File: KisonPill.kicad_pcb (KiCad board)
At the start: 4 copper layers, 49 x 48 mm, 44 parts, among them J1 USB_C_Receptacle_USB2.0, J2 Conn_01x17_Male, J3 Conn_01x17_Male, J4 Conn_01x03_Male, J5 Conn_01x04_Male, J6 Conn_01x03_Male, J7 Conn_01x08_Male, Q1 2N3904S-RTK/PS, Q2 2N3904S-RTK/PS, SW1 SW_Push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

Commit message: Add Elaina
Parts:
- added G***: LOGO, KisonCommon:ElainaLogo, B.Cu at (146.8, 103.6)
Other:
- board text added: "3V3"
- board text added: "EXT_5V"
- board text added: "GND"
- board text added: "JLCJLCJLCJLC"
- board text added: "KisonHe KisonPillV0.1"

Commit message: save
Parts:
- removed G***: LOGO, KisonCommon:ElainaLogo
- added R14: 0, Resistor_SMD:R_0603_1608Metric, F.Cu at (150.2, 84.3)
- added R15: 0, Resistor_SMD:R_0603_1608Metric, F.Cu at (152.0, 84.2)
- added U7: ESP32FullConnector, Connector_Molex:Molex_CLIK-Mate_502382-1270_1x12-1MP_P1.25mm_Vertical, B.Cu at (160.1, 112.8)
- U4: value ESP32JtagConnector -> ESP32FullConnector-KisonCommon; footprint KisonCommon:jtag1.27 -> KisonCommon:jtag1.27-12
- U6: moved to B.Cu
- moved D5 5.57 mm to (143.4, 120.4), turned to 0 degrees
- moved SW1 4.63 mm to (146.8, 121.0), turned to 0 degrees
- moved C8 3.67 mm to (157.4, 85.2), turned to 270 degrees
- moved U6 3.43 mm to (143.3, 118.0), turned to 270 degrees
- moved J6 3.40 mm to (154.4, 114.3)
- moved J5 2.72 mm to (150.6, 112.1)
- moved J4 2.10 mm to (146.9, 114.2)
- moved C9 0.43 mm to (155.0, 84.5), turned to 270 degrees
- moved U4 0.16 mm to (136.9, 83.6)
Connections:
- J7 pad 6: /IO15 -> /IO32
- Q2 pad 1: /IO0 -> /DTR
- Q2 pad 3: /DTR -> /IO0
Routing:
- net /IO32: track 11.9 -> 62.0 mm, vias 0 -> 1
- net /EXT_5V: track 39.4 -> 88.3 mm
- net /EN: track 134.0 -> 94.5 mm
- net +3V3: track 189.8 -> 168.3 mm, vias 5 -> 6
- net GND: track 335.2 -> 314.3 mm
- net /IO15: track 69.8 -> 51.1 mm
- net /IO12: track 46.6 -> 34.1 mm
- net /IO14: track 40.3 -> 30.9 mm
- net Net-(D5-Pad2): track 8.50 -> 13.4 mm
- net /IO0: track 77.0 -> 72.4 mm
- net /DTR: track 41.7 -> 39.2 mm
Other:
- board size 49 x 48 mm -> 44.7 x 46.8 mm

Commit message: V1
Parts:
- removed C10, C9: 0.1uf, Capacitor_SMD:C_0603_1608Metric
- removed C8: 10uf, Capacitor_SMD:C_1206_3216Metric
- removed J4, J6: Conn_01x03_Male, Connector_PinHeader_2.54mm:PinHeader_1x03_P2.54mm_Vertical
- removed J5: Conn_01x04_Male, Connector_PinHeader_2.54mm:PinHeader_1x04_P2.54mm_Vertical
- removed J7: Conn_01x08_Male, Connector_PinHeader_2.54mm:PinHeader_1x08_P2.54mm_Vertical
- removed U5: ICM-20602, Package_LGA:LGA-16_3x3mm_P0.5mm_LayoutBorder3x5y
- added G***: LOGO, KisonCommon:tamako100, B.Cu at (133.6, 96.8)
- C5, C6, C7, R13, R2, R3, U3, U4, U7: moved to F.Cu
- J2, J3: value Conn_01x17_Male -> Conn_01x19_Male; footprint Connector_PinHeader_2.54mm:PinHeader_1x17_P2.54mm_Vertical -> Connector_PinHeader_2.54mm:PinHeader_1x19_P2.54mm_Vertical
- U2: moved to B.Cu
- U6: footprint KisonCommon:USBLC6-2P6 -> KisonCommon:USBLC6-2P6-SOT666
- moved U7 48.1 mm to (134.4, 72.1), turned to 0 degrees
- moved R6 37.1 mm to (125.9, 102.1), turned to 90 degrees
- moved J2 28.8 mm to (147.0, 70.0)
- moved D5 27.9 mm to (125.8, 98.8), turned to 270 degrees
- moved C4 27.6 mm to (128.6, 87.7), turned to 0 degrees
- moved R12 23.8 mm to (138.2, 90.6), turned to 90 degrees
- moved Q1 22.0 mm to (141.3, 89.2), turned to 90 degrees
- moved U3 20.5 mm to (132.2, 93.1), turned to 180 degrees
- moved C3 19.3 mm to (135.4, 87.7), turned to 180 degrees
- moved R2 18.8 mm to (127.9, 102.0)
- moved R3 18.0 mm to (127.9, 98.8)
- moved R15 17.4 mm to (136.2, 76.7), turned to 180 degrees
- moved Q2 14.9 mm to (141.4, 93.1), turned to 270 degrees
- moved R11 14.6 mm to (144.2, 90.8), turned to 270 degrees
- moved U2 13.8 mm to (134.4, 77.6), turned to 180 degrees
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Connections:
- J2 pad 1: /EN -> +3V3
- J2 pad 10: /IO27 -> /IO26
- J2 pad 11: /IO14 -> /IO27
- J2 pad 12: /IO12 -> /IO14
- J2 pad 13: GND -> /IO12
- J2 pad 14: /IO13 -> GND
- J2 pad 15: /SD2 -> /IO13
- J2 pad 16: /SD3 -> /SD2
- J2 pad 17: /CMD -> /SD3
- J2 pad 2: /SENSOR_VP -> /EN
- J2 pad 3: /SENSOR_VN -> /SENSOR_VP
- J2 pad 4: /IO34 -> /SENSOR_VN
- J2 pad 5: /IO35 -> /IO34
- J2 pad 6: /IO32 -> /IO35
- J2 pad 7: /IO33 -> /IO32
- J2 pad 8: /IO25 -> /IO33
- J2 pad 9: /IO26 -> /IO25
- J3 pad 1: /IO23 -> GND
- J3 pad 10: /IO16 -> /IO5
- J3 pad 11: /IO4 -> /IO17
- J3 pad 12: /IO0 -> /IO16
- J3 pad 13: /IO2 -> /IO4
- J3 pad 14: /IO15 -> /IO0
- J3 pad 15: /SD1 -> /IO2
- J3 pad 16: /SD0 -> /IO15
- J3 pad 17: /CLK -> /SD1
- J3 pad 2: /IO22 -> /IO23
- J3 pad 3: /TXD0 -> /IO22
- J3 pad 4: /RXD0 -> /TXD0
- J3 pad 5: /IO21 -> /RXD0
- J3 pad 6: /IO19 -> /IO21
- J3 pad 7: /IO18 -> GND
- J3 pad 8: /IO5 -> /IO19
- J3 pad 9: /IO17 -> /IO18
- U4 pad 8: /EXT_5V -> Net-(U4-Pad8)
- U7 pad 10: /RXD0 -> Net-(R14-Pad1)
- U7 pad 8: /EXT_5V -> Net-(U7-Pad8)
- U7 pad 9: /TXD0 -> Net-(R15-Pad2)
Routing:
- net GND: track 314.3 -> 231.8 mm, vias 6 -> 5
- net /IO32: track 62.0 -> 9.41 mm, vias 1 -> 0
- net /IO0: track 72.4 -> 122.8 mm, vias 2 -> 3
- net +3V3: track 168.3 -> 118.6 mm
- net /IO35: track 56.0 -> 8.14 mm
- net /IO23: track 50.1 -> 5.09 mm, vias 3 -> 0
- net /IO18: track 52.9 -> 13.3 mm, vias 1 -> 0
- net /IO5: track 47.5 -> 14.6 mm, vias 1 -> 0
- net /EXT_5V: track 88.3 -> 57.3 mm, vias 1 -> 2
- net /TXD0: track 28.5 -> 56.9 mm
- net /IO4: track 50.3 -> 22.4 mm
- net /IO19: track 38.5 -> 12.0 mm, vias 2 -> 0
- net /TXD: track 29.2 -> 4.23 mm, vias 2 -> 0
- net /RXD0: track 27.1 -> 51.2 mm
- net /RXD: track 28.5 -> 6.00 mm, vias 2 -> 0
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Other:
- board size 44.7 x 46.8 mm -> 30.5 x 50 mm
- board text added: "0"
- board text added: "12"
- board text added: "13"
- board text added: "14"
- board text added: "15"
- board text added: "16"
- board text added: "17"
- board text added: "18"
- board text added: "19"
- board text added: "2"
- board text added: "21"
- board text added: "22"
- board text added: "23"
- board text added: "25"
- board text added: "26"
- board text added: "27"
- board text added: "32"
- board text added: "33"
- board text added: "34"
- board text added: "35"
- board text added: "4"
- board text added: "5"
- board text added: "5V"
- board text added: "EN"
- board text added: "IO0"
- board text added: "RX"
- board text added: "TX"
- board text removed: "EXT_5V"

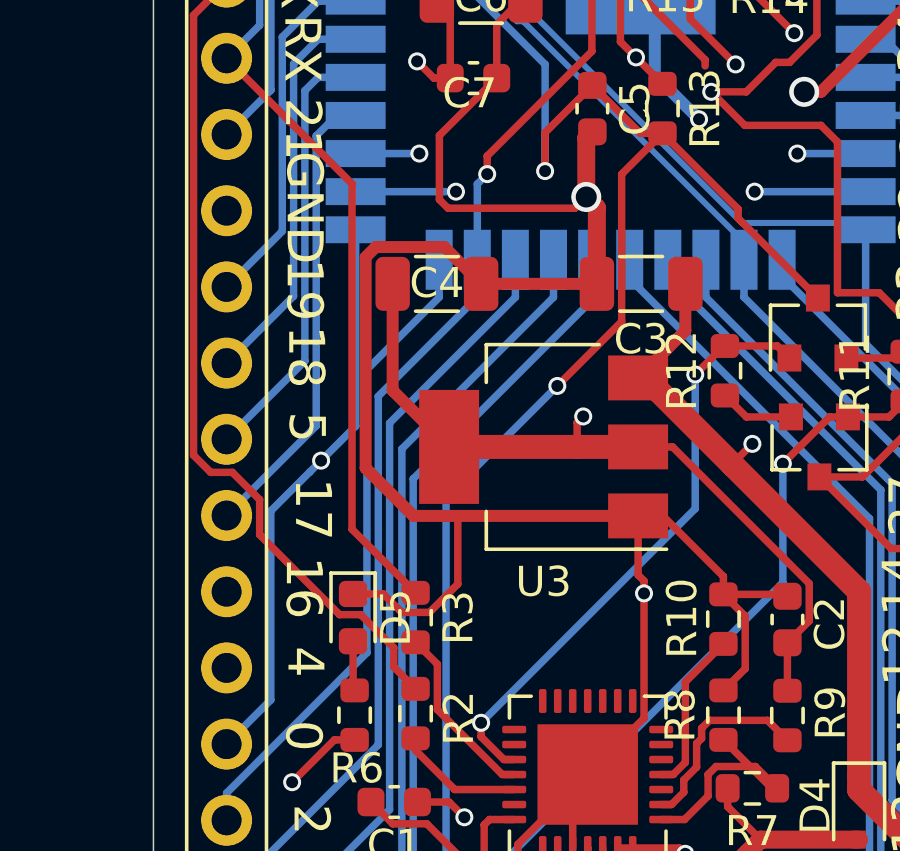
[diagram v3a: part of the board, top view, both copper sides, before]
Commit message: Fix Error Over RX&TX
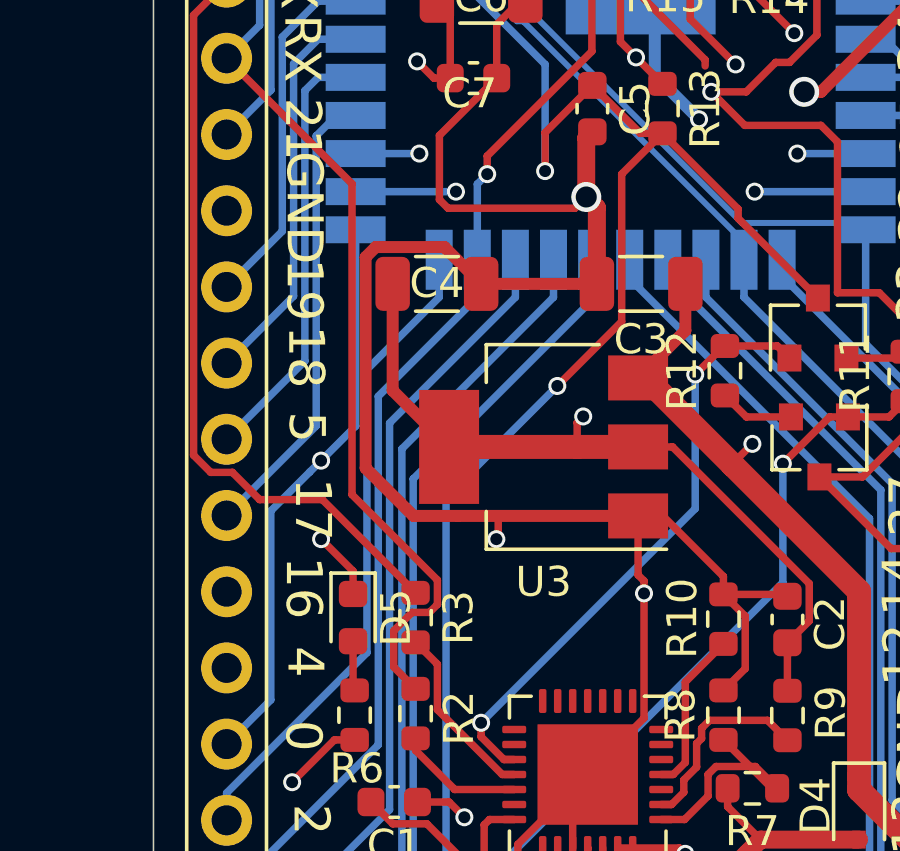
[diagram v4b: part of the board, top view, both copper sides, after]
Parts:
- removed G***: LOGO, KisonCommon:tamako100
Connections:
- R2 pad 2: /TXD0 -> /RXD0
- R3 pad 1: /RXD0 -> /TXD0
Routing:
- net /RXD0: track 51.2 -> 56.0 mm
- net GND: track 231.8 -> 234.4 mm, vias 5 -> 7
- net /TXD0: track 56.9 -> 54.5 mm

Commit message: V2
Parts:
- U4: footprint KisonCommon:jtag1.27-12 -> KisonCommon:jtag1.27-10
- U7: footprint Connector_Molex:Molex_CLIK-Mate_502382-1270_1x12-1MP_P1.25mm_Vertical -> Connector_Molex:Molex_CLIK-Mate_502382-1070_1x10-1MP_P1.25mm_Vertical
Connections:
- net /RXD renamed /CP2102RX
- net /RXD0 renamed /ESPRX
- net /TXD renamed /CP2102TX
- net /TXD0 renamed /ESPTX
- U4 pad 8: Net-(U4-Pad8) -> /IO0
- U7 pad 8: Net-(U7-Pad8) -> /IO0
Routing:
- net GND: track 234.4 -> 243.7 mm
- net /IO0: track 122.8 -> 131.7 mm, vias 3 -> 4
- net Net-(R15-Pad2): track 11.1 -> 15.0 mm
- net /EN: track 95.7 -> 93.9 mm
- net +3V3: track 118.6 -> 119.4 mm
- net /IO12: track 44.0 -> 43.3 mm
- net /IO14: track 41.1 -> 40.6 mm
- net /IO13: track 47.0 -> 47.5 mm

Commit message: Improve Texts
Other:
- board text added: "1"
- board text added: "10"
- board text added: "KisonHe KisonPill2"
- board text removed: "KisonHe KisonPillV0.1"

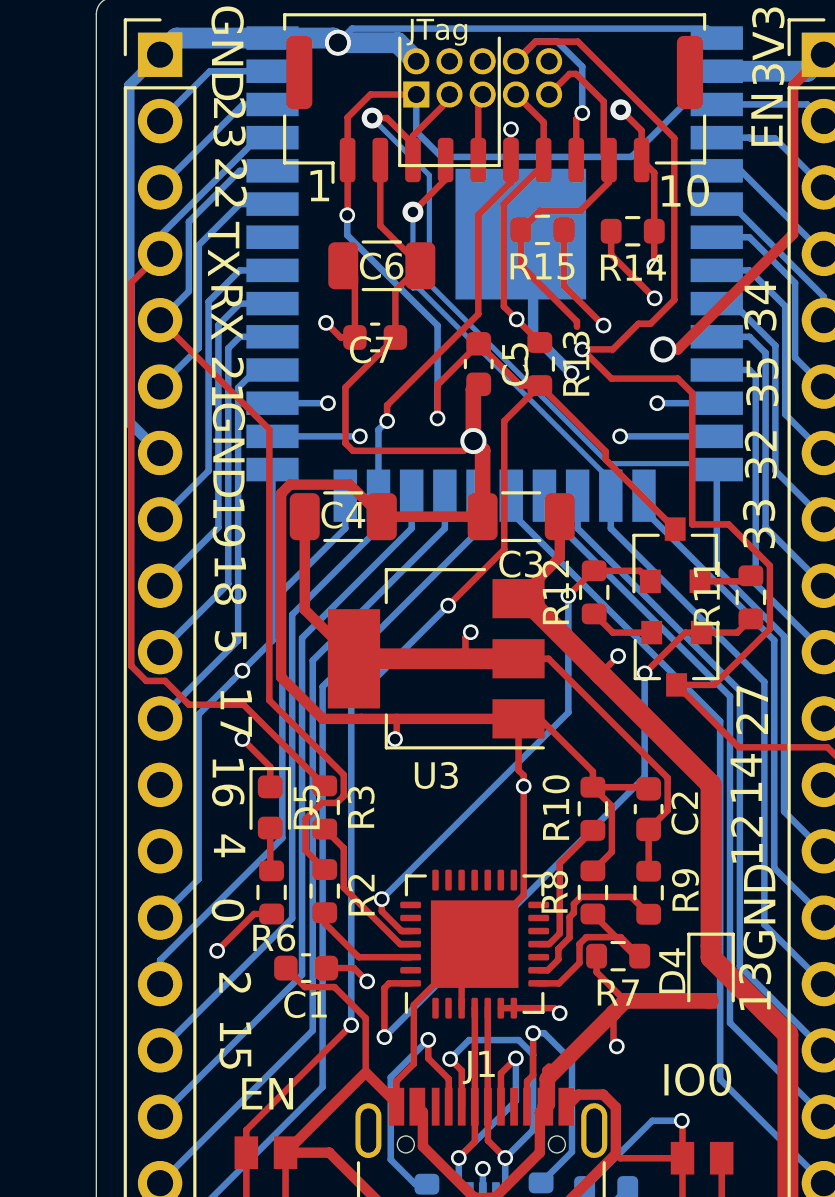
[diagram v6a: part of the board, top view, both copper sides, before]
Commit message: Added a switch to pick TX
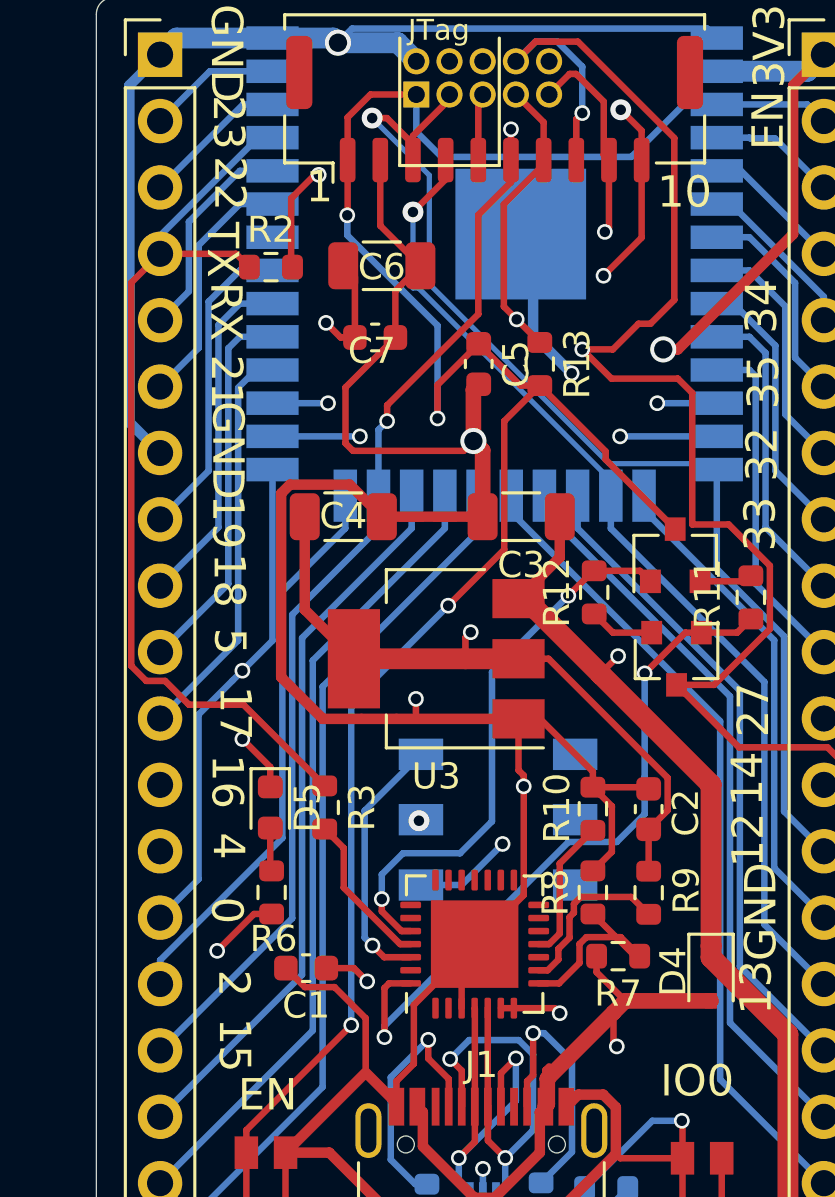
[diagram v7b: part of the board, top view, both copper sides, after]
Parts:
- removed R14, R15: 0, Resistor_SMD:R_0603_1608Metric
- added SW3: SW_Push_DPDT, KisonCommon:MSS22D18G2, B.Cu at (134.6, 99.2)
- moved R2 24.0 mm to (125.9, 78.1), turned to 0 degrees
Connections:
- net Net-(R14-Pad1) renamed /FT2232TX
- R2 pad 1: /CP2102TX -> /ESPTX
- R2 pad 2: /ESPRX -> /FT2232RX
- U4 pad 9: Net-(R15-Pad2) -> /FT2232RX
- U7 pad 9: Net-(R15-Pad2) -> /FT2232RX
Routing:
- net /FT2232TX: track 11.5 -> 42.3 mm, vias 2 -> 3
- net /FT2232RX: track 0.00 -> 24.2 mm, vias 0 -> 2
- net /ESPTX: track 54.5 -> 35.7 mm, vias 1 -> 0
- net /ESPRX: track 56.0 -> 38.4 mm
- net Net-(R15-Pad2): track 15.0 -> 0.00 mm
- net /CP2102TX: track 4.23 -> 10.0 mm, vias 0 -> 1
- net GND: track 243.7 -> 245.1 mm
- net /RTS: track 20.3 -> 21.5 mm
- net /DTR: track 25.9 -> 27.0 mm
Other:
- board text added: "CP2102"
- board text added: "FT2232"
- board text added: "KisonHe KisonPill3"
- board text removed: "KisonHe KisonPill2"

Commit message: Fix Direction Errors
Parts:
- moved U4 5.18 mm to (136.4, 70.1), turned to 270 degrees
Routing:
- net +3V3: track 119.4 -> 135.6 mm
- net /IO15: track 55.2 -> 43.3 mm, vias 2 -> 1
- net /IO14: track 40.6 -> 49.0 mm, vias 1 -> 3
- net /FT2232TX: track 42.3 -> 48.9 mm, vias 3 -> 2
- net /IO12: track 43.3 -> 48.3 mm
- net /IO13: track 47.5 -> 44.9 mm
- net /IO0: track 131.7 -> 129.5 mm
- net GND: track 245.1 -> 246.8 mm, vias 7 -> 8
- net /FT2232RX: track 24.2 -> 25.4 mm
- net /EN: track 93.9 -> 94.8 mm
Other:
- board text added: "KisonHe KisonPillV4"
- board text removed: "KisonHe KisonPill3"
